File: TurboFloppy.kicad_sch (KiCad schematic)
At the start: 13 parts, among them J1 C16-Exp-Port, J2 SOCKET_28PIN, Q1 NPN, U1 8255, U2 74LS30, U4 74LS27, U5 74LS10

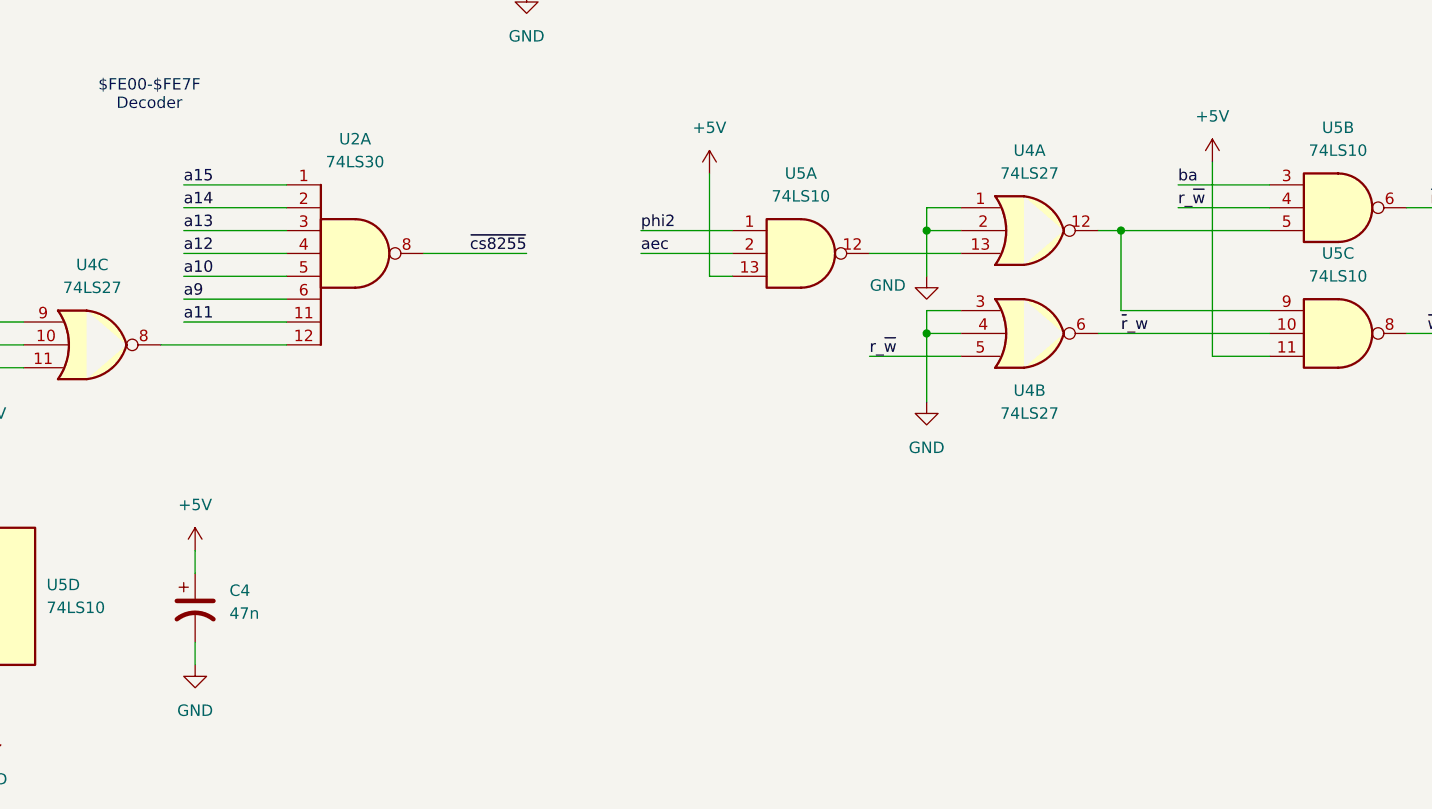
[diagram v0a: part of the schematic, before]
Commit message: Add decoupling caps
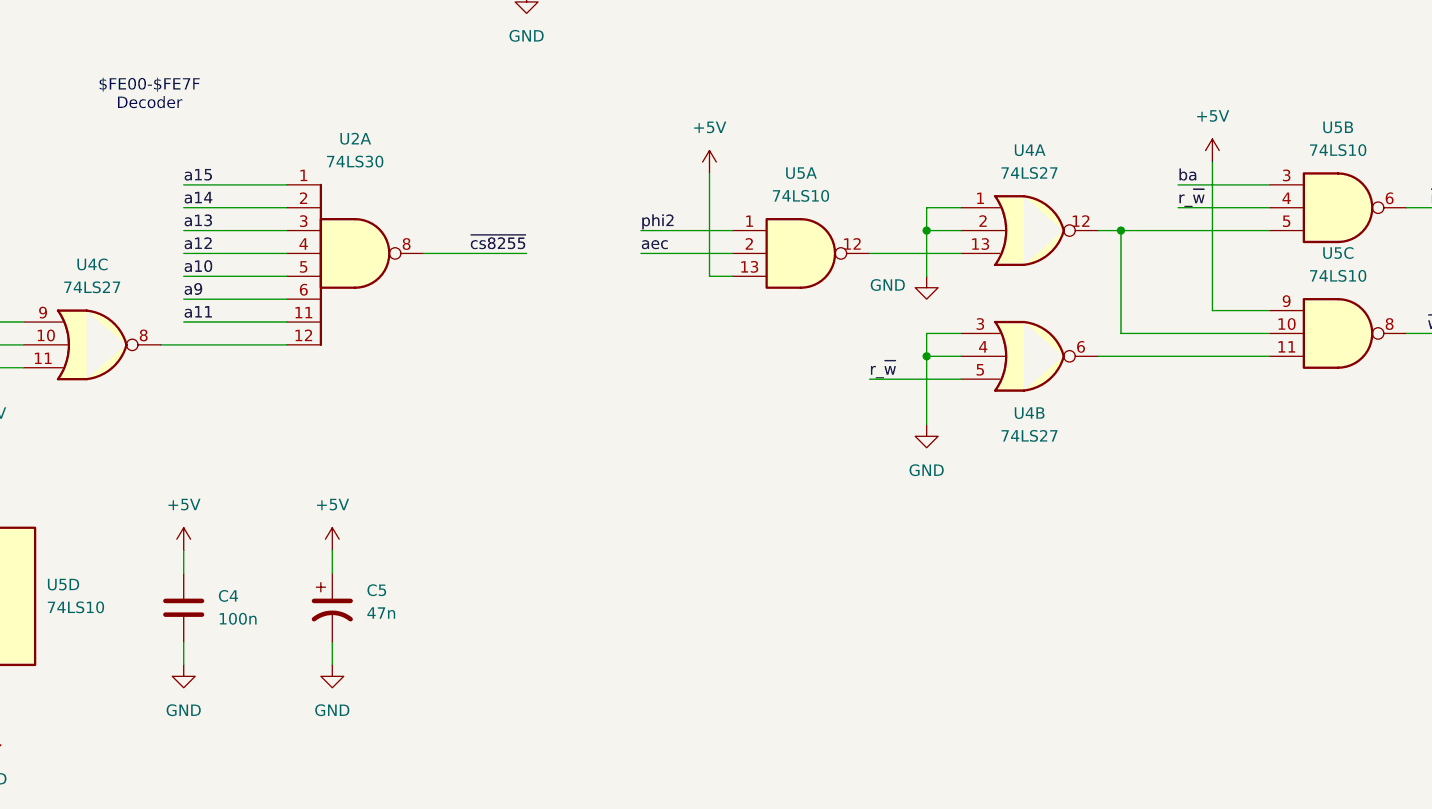
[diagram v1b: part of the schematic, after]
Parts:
- added C4: 100n, Capacitor_THT:C_Disc_D7.0mm_W2.5mm_P5.00mm, symbol Device:C
- C1, C2, C3: footprint (none) -> Capacitor_THT:C_Disc_D7.0mm_W2.5mm_P5.00mm
- C5: renamed from C4; footprint (none) -> Capacitor_THT:CP_Radial_D5.0mm_P2.00mm
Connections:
- net +5V: now also U5.9, C4.1; no longer U5.11
- net GND: now also C4.2
- net at U4.12, U5.5: now also U5.10; no longer U5.9
- net ~{r}_w: no longer names the net of U4.6
- net ~{r}_w: now also U5.11; no longer U5.10
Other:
- moved on the sheet: C5, U4B

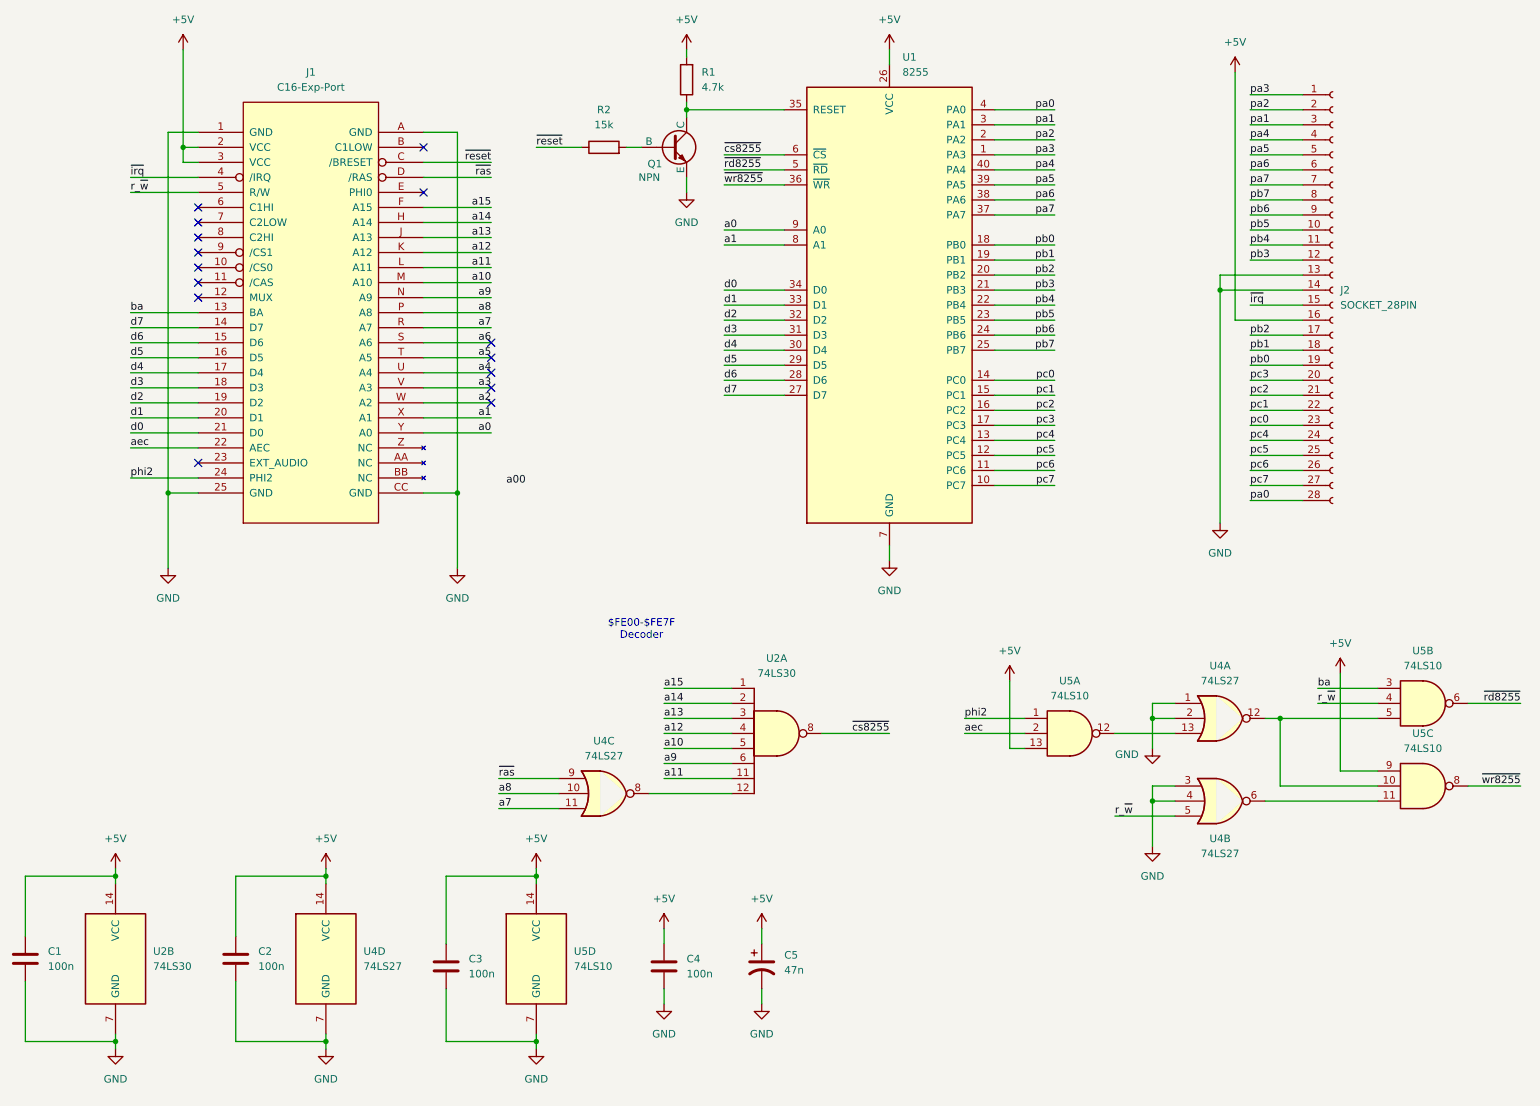
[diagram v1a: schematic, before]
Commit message: Add alternative pin header
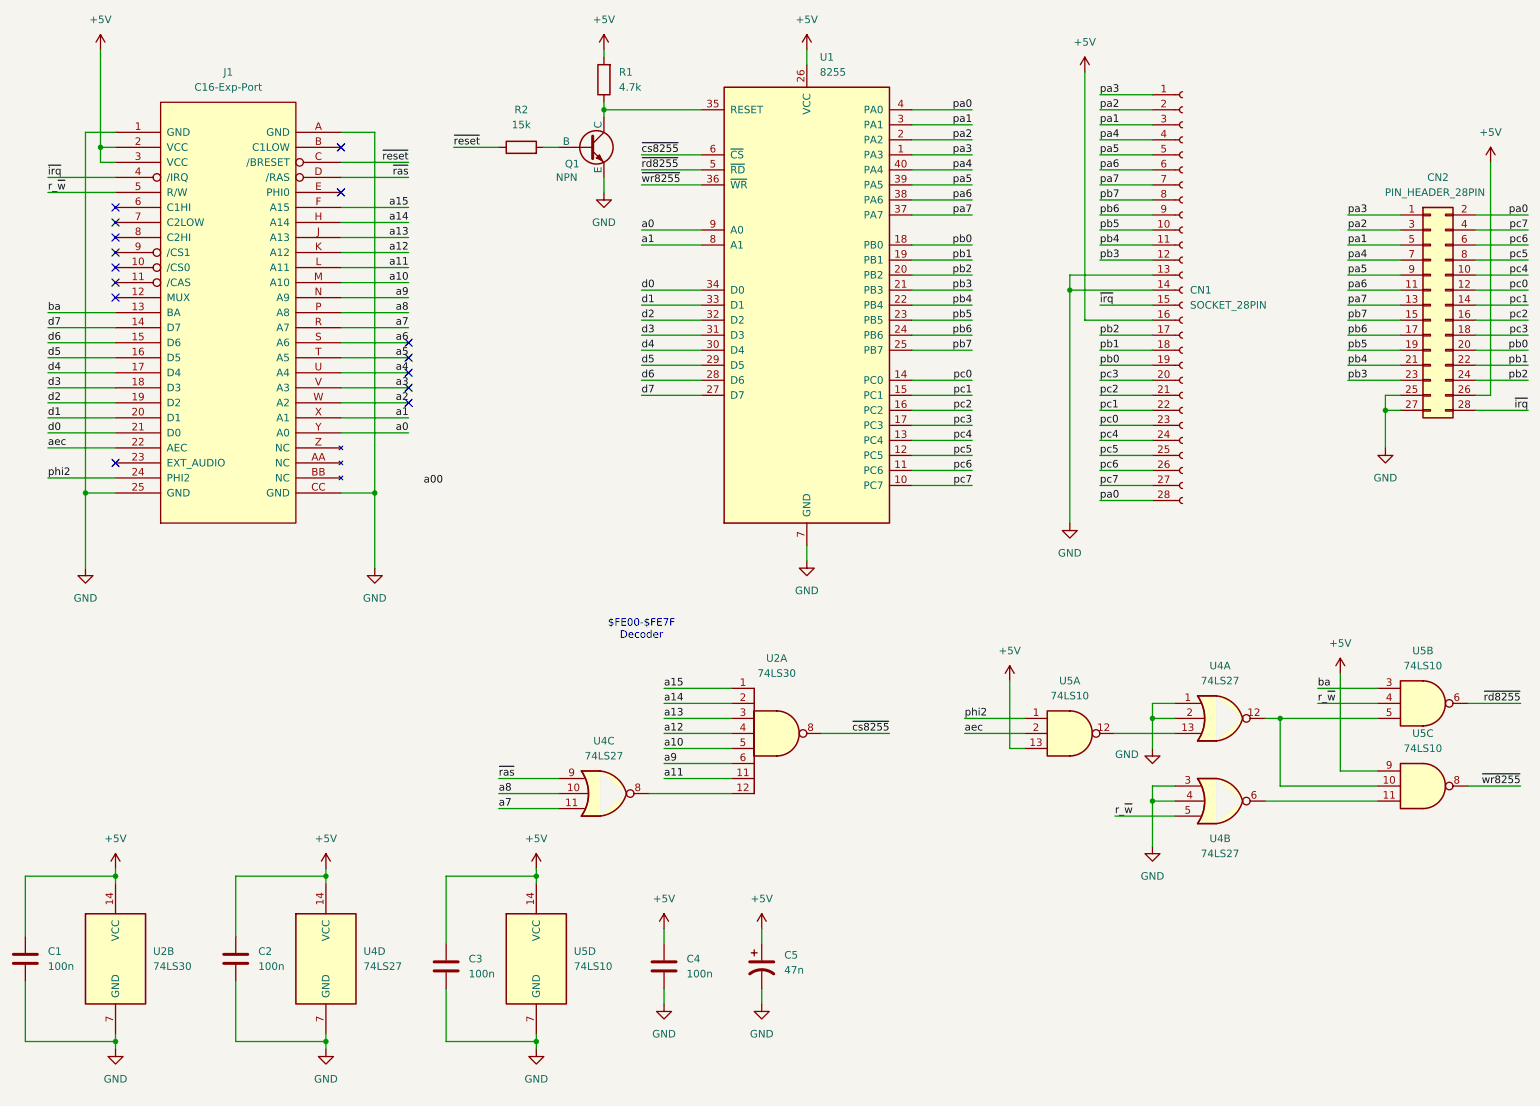
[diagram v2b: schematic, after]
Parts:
- added CN2: PIN_HEADER_28PIN, Connector_PinHeader_2.54mm:PinHeader_2x14_P2.54mm_Vertical, symbol Connector_Generic:Conn_02x14_Odd_Even
- renumbered J2 to CN1
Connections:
- net +5V: now also CN2.26 (Pin_26)
- net GND: now also CN2.25 (Pin_25), CN2.27 (Pin_27)
- net pa0: now also CN2.2 (Pin_2)
- net pa1: now also CN2.5 (Pin_5)
- net pa2: now also CN2.3 (Pin_3)
- net pa3: now also CN2.1 (Pin_1)
- net pa4: now also CN2.7 (Pin_7)
- net pa5: now also CN2.9 (Pin_9)
- net pa6: now also CN2.11 (Pin_11)
- net pa7: now also CN2.13 (Pin_13)
- net pb0: now also CN2.20 (Pin_20)
- net pb1: now also CN2.22 (Pin_22)
- net pb2: now also CN2.24 (Pin_24)
- net pb3: now also CN2.23 (Pin_23)
- net pb4: now also CN2.21 (Pin_21)
- net pb5: now also CN2.19 (Pin_19)
- net pb6: now also CN2.17 (Pin_17)
- net pb7: now also CN2.15 (Pin_15)
- net pc0: now also CN2.12 (Pin_12)
- net pc1: now also CN2.14 (Pin_14)
- net pc2: now also CN2.16 (Pin_16)
- net pc3: now also CN2.18 (Pin_18)
- net pc4: now also CN2.10 (Pin_10)
- net pc5: now also CN2.8 (Pin_8)
- net pc6: now also CN2.6 (Pin_6)
- net pc7: now also CN2.4 (Pin_4)
- net ~{irq}: now also CN2.28 (Pin_28)
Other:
- moved on the sheet: CN1, J1, Q1, R1, R2, U1

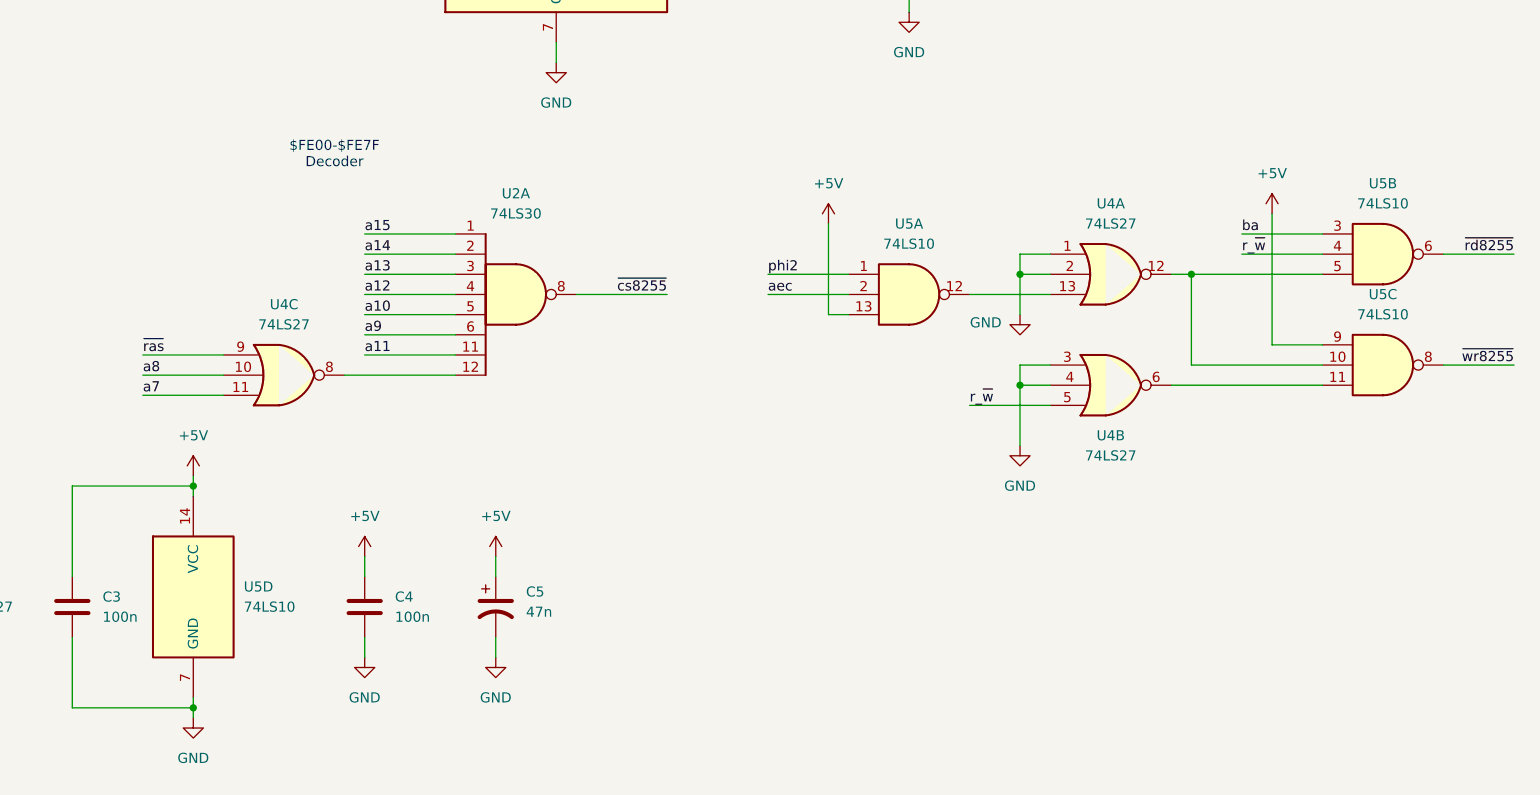
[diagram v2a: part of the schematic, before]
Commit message: Make less than 10x10cm and add screw holes
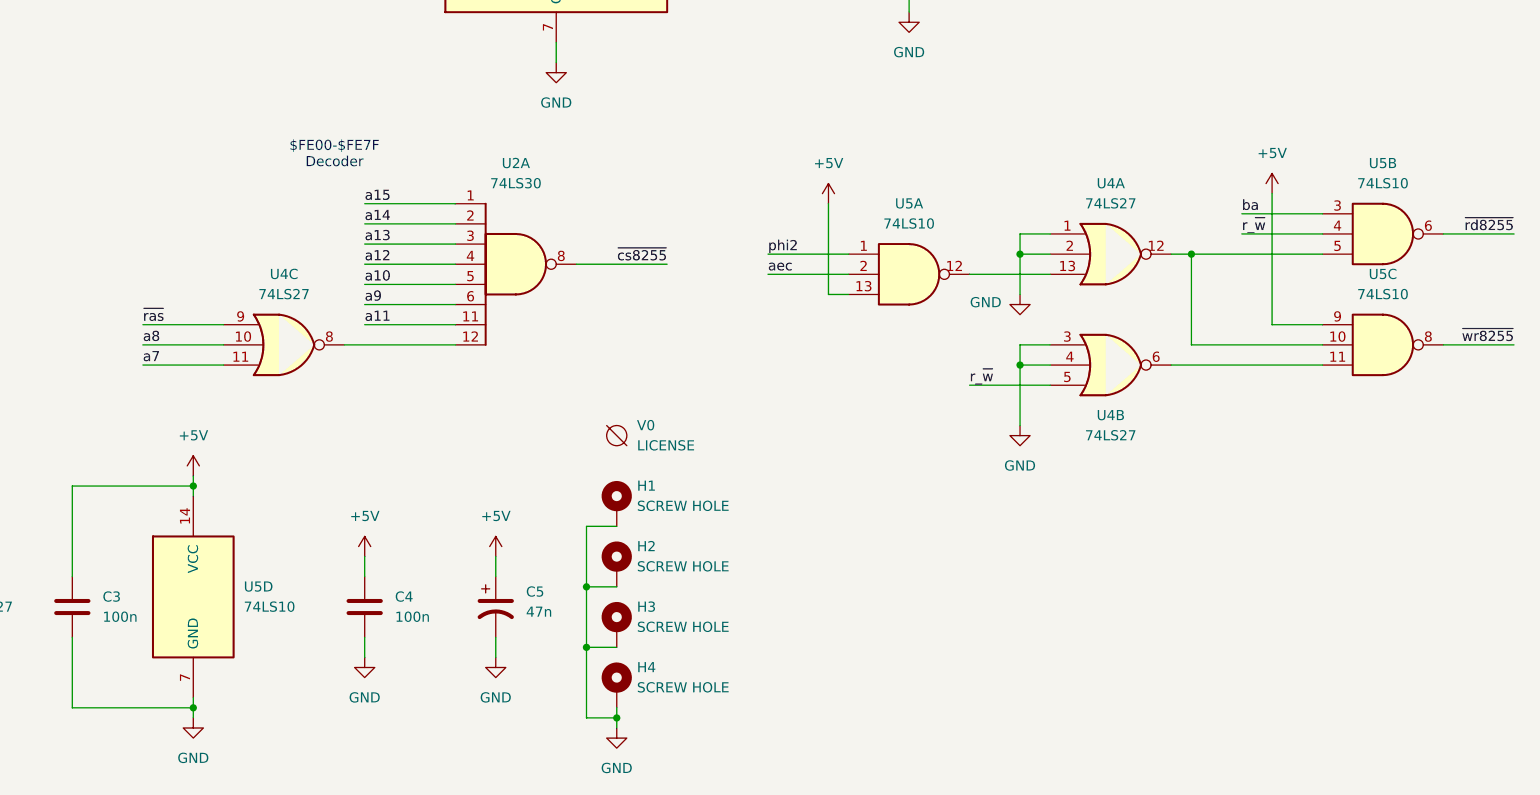
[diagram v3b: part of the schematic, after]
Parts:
- added H1, H2, H3, H4: SCREW HOLE, MountingHole:MountingHole_3.2mm_M3_Pad, symbol Mechanical:MountingHole_Pad
- added V0: LICENSE, TurboFloppy:cc_by_nc_sa, symbol void:Void
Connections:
- net GND: now also H1.1, H2.1, H3.1, H4.1
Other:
- moved on the sheet: U2A, U4A, U4B, U4C, U5A, U5B, U5C
